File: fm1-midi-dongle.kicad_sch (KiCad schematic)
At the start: 30 parts, among them J1 TYPE-C 24P-GTJB 040, J2 TYPE-C-31-M-12, J3 PJ-320D, J4 PJ-320D, U1 CH32X035G8U6, U2 XC6206P332MR, U3 SY6280AAC, U4 H11L1SM, U5 SN74LVC1G3157

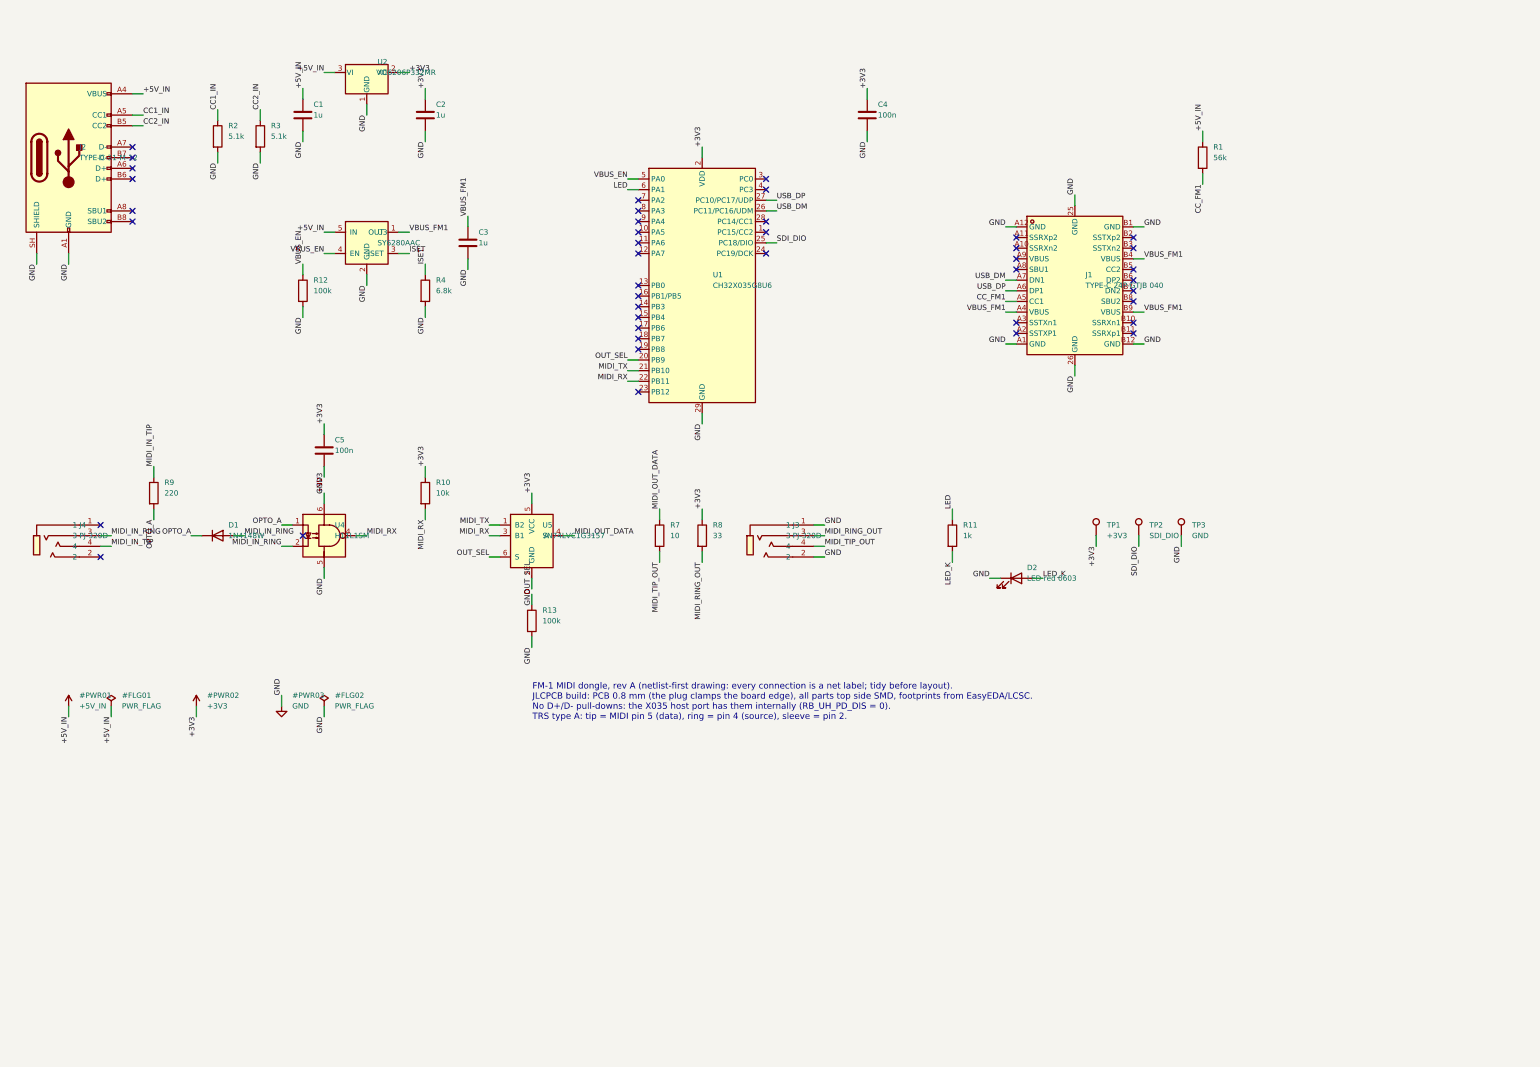
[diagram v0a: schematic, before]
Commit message: v5: USB-A host port on the bottom face, schematic cleanup, hand-routed
- J1 = USB-A receptacle 911-321B2028S10100 (LCSC C42474) on B.Cu, mouth 0.8 mm
  past the top edge; board still 20 x 37.7 mm. Plug, R1 and CC_FM1 removed,
  VBUS_HOST, C3 now 10 uF (C96446) host-port bulk.
- Schematic: power/ground as KiCad power symbols, no overlapping symbols or
  texts (generator checks it), clean symbols for SY6280, 3157, USB-A, PJ-320D.
- THRU switch inputs swapped (B2 = MIDI_RX, B1 = MIDI_TX) and R13 is now a
  pull-up: THRU still default; firmware drives PB9 low for MCU MIDI.
- Floorplan + hand-written routing (tools/route.py): DRC 0 unconnected, house
  style clean, 0 loops. One track_width neck at U1 VDD (0.4 mm pitch).
- TP3 (GND) moved to the top-left corner; opto block 2.1 mm lower.
- Renders, BOM and DESIGN.md updated.

Co-Authored-By: Claude Opus 5.5 <noreply@anthropic.com>
Claude-Session: https://claude.ai/code/session_01Dtfv3zuhZTs975LiSXznFQ
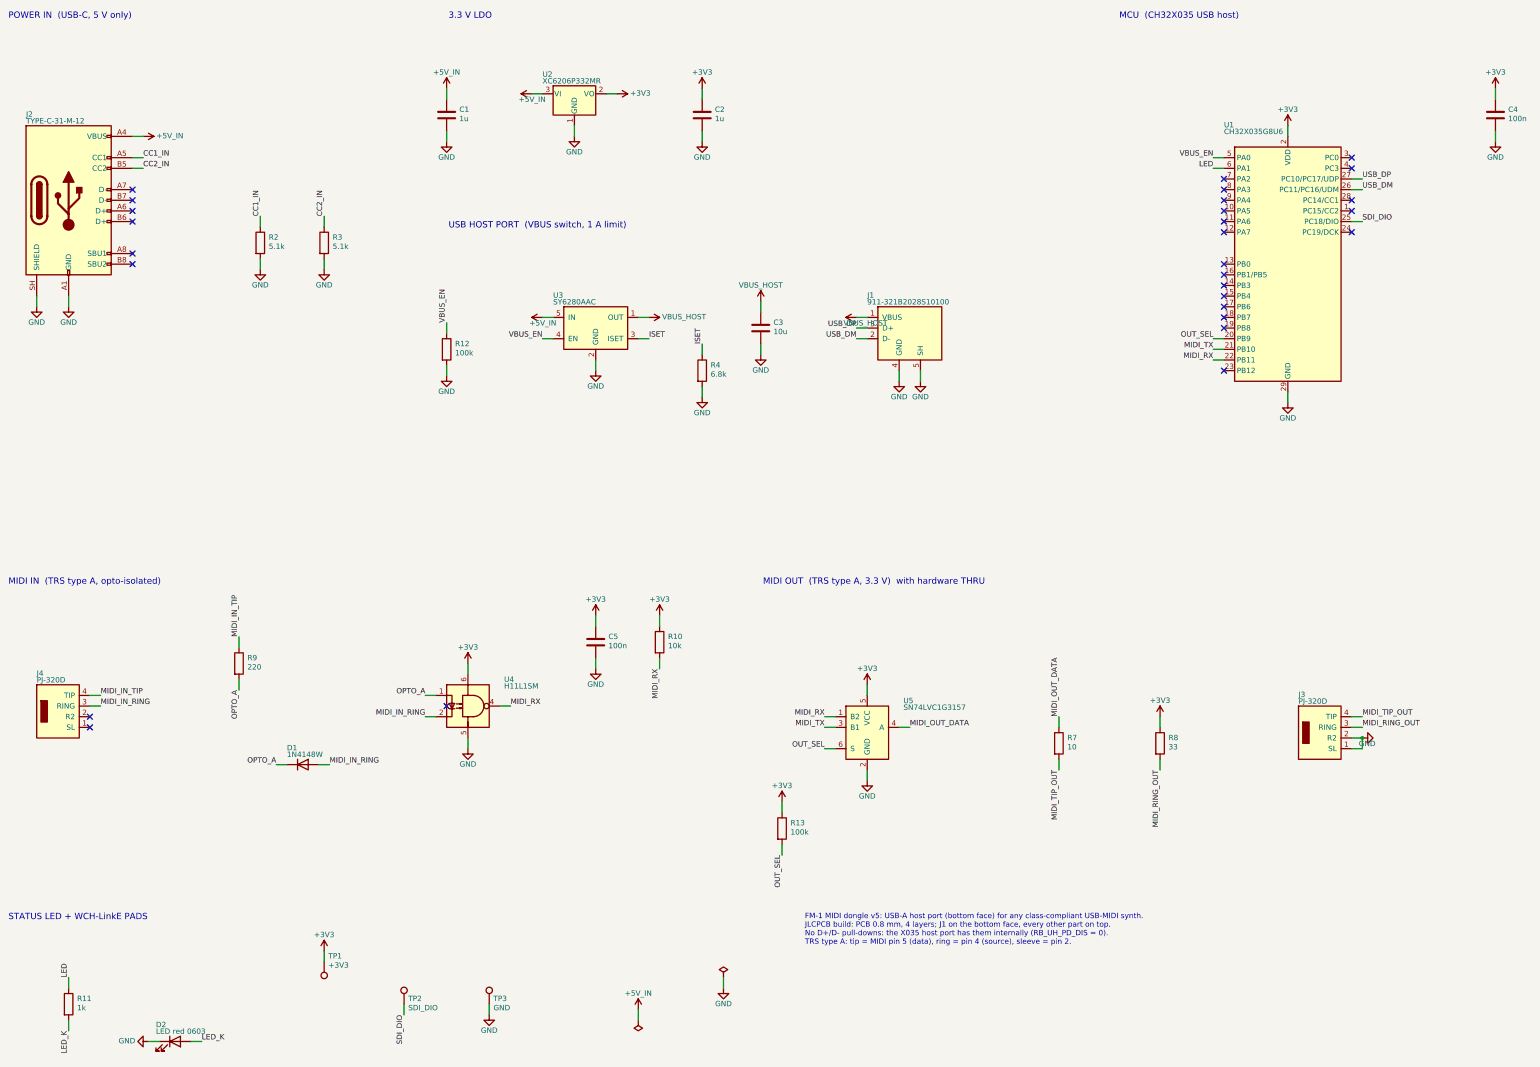
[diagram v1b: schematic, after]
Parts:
- removed D1: 1N4148W, Diode_SMD:D_SOD-123, symbol Device:D
- removed J1: TYPE-C 24P-GTJB 040, fm1_dongle:USB-C-SMD_TYPE-C-24P-GTJB-040, symbol fm1_dongle:USB-C_Plug_GTJB040
- removed R9: 220, Resistor_SMD:R_0603_1608Metric, symbol Device:R
- removed TP3: GND, TestPoint:TestPoint_Pad_1.5x1.5mm, symbol Connector:TestPoint
- added J1: 911-321B2028S10100, fm1_dongle:USB-A-SMD_911-321B2028S10100, symbol fm1_dongle:USB_A_911-321B2028S10100
- added TP2: SDI_DIO, TestPoint:TestPoint_Pad_1.5x1.5mm, symbol Connector:TestPoint
- added U5: SN74LVC1G3157, Package_TO_SOT_SMD:SOT-363_SC-70-6, symbol fm1_dongle:SN74LVC1G3157
- C3: value 1u -> 10u; LCSC# C15849 -> C96446; MPN CL10A105KB8NNNC -> CL10A106MA8NRNC; Note (none) -> bulk on the host port: a synth hot-plugged into J1 charges 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
- D1: renamed from U5; value SN74LVC1G3157 -> 1N4148W; footprint Package_TO_SOT_SMD:SOT-363_SC-70-6 -> Diode_SMD:D_SOD-123; symbol fm1_dongle:SN74LVC1G3157 -> Device:D; LCSC# C38663 -> C81598; MPN SN74LVC1G3157DCKR -> 1N4148W; Note TI SCES424O: 1 B2, 2 GND, 3 B1, 4 A, 5 VCC, 6 S; S low A=B1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 -> reverse-polarity protection across the opto LED
- R13: Note OUT_SEL default low = hardware THRU until firmware drives P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 -> OUT_SEL pull-up: default high = hardware THRU until firmwar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
- R9: renamed from R1; value 56k -> 220; LCSC# C23206 -> C22962; MPN 0603WAF5602T5E -> 0603WAF2200T5E; Note Rp: the FM-1 sees a default-USB host -> (none)
- TP3: renamed from TP2; value SDI_DIO -> GND
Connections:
- net CC_FM1 is gone; now on net OPTO_A: R9.2
- net +3V3: now also R13.1, U5.5 (VCC); no longer D1.5 (VCC)
- net +5V_IN: no longer R9.1
- net GND: now also TP3.1, J1.4 (GND), J1.5 (SH), J1.6 (SH), J1.7 (SH), J1.8 (SH), U5.2 (GND); no longer D1.2 (GND), R13.2
- net MIDI_IN_RING: now also D1.2 (A)
- net MIDI_IN_TIP: now also R9.1
- net MIDI_OUT_DATA: now also U5.4 (A); no longer D1.4 (A)
- net MIDI_RX: now also U5.1 (B2); no longer D1.3 (B1)
- net MIDI_TX: now also U5.3 (B1); no longer D1.1 (B2)
- net OPTO_A: now also D1.1 (K)
- net OUT_SEL: now also R13.2, U5.6 (S); no longer D1.6 (S), R13.1
- net SDI_DIO: now also TP2.1; no longer TP3.1
- net USB_DM: now also J1.2 (D-)
- net USB_DP: now also J1.3 (D+)
- net VBUS_FM1 renamed VBUS_HOST
- net VBUS_HOST: now also J1.1 (VBUS)
- no-connect marks 42 -> 28
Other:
- note added: "3.3 V LDO"
- note added: "FM-1 MIDI dongle v5: USB-A host port (bottom face) for any class-compliant USB-MIDI synth. JLCPCB build: PCB 0.8 mm, 4 layers; J1 on the bottom face, every other part on top. No D+/D- pull-downs: the X035 host port has them internally (RB_UH_PD_DIS = 0). TRS type A: tip = MIDI pin 5 (data), ring = pin 4 (source), sleeve = pin 2."
- note added: "MCU (CH32X035 USB host)"
- note added: "MIDI IN (TRS type A, opto-isolated)"
- note added: "MIDI OUT (TRS type A, 3.3 V) with hardware THRU"
- note added: "POWER IN (USB-C, 5 V only)"
- note added: "STATUS LED + WCH-LinkE PADS"
- note added: "USB HOST PORT (VBUS switch, 1 A limit)"
- note removed: "FM-1 MIDI dongle, rev A (netlist-first drawing: every connection is a net label; tidy before layout). JLCPCB build: PCB 0.8 mm (the plug clamps the board edge), all parts top side SMD, footprints from EasyEDA/LCSC. No D+/D- pull-downs: the X035 host port has them internally (RB_UH_PD_DIS = 0). TRS type A: tip = MIDI pin 5 (data), ring = pin 4 (source), sleeve = pin 2."
- moved on the sheet: R9, TP3
